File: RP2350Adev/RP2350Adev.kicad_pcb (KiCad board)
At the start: 2 copper layers, 32.6 x 53.6 mm, 44 parts, among them J1 USB4105-GF-A, J2 LEFT, J3 DEBUG, J4 RIGHT, U1 W25Q32JV, U2 RP2350A, U3 MCP1702T-3302E_CB, X1 IQXO-791

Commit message: Add files via upload
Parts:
- moved C10 0.30 mm to (156.9, 87.9)
- moved S2 0.29 mm to (148.4, 86.7)
- moved C17 0.18 mm to (155.3, 83.2)
- moved C11 0.15 mm to (156.9, 89.8)
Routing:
- net GND: track 88.4 -> 69.3 mm, vias 25 -> 22

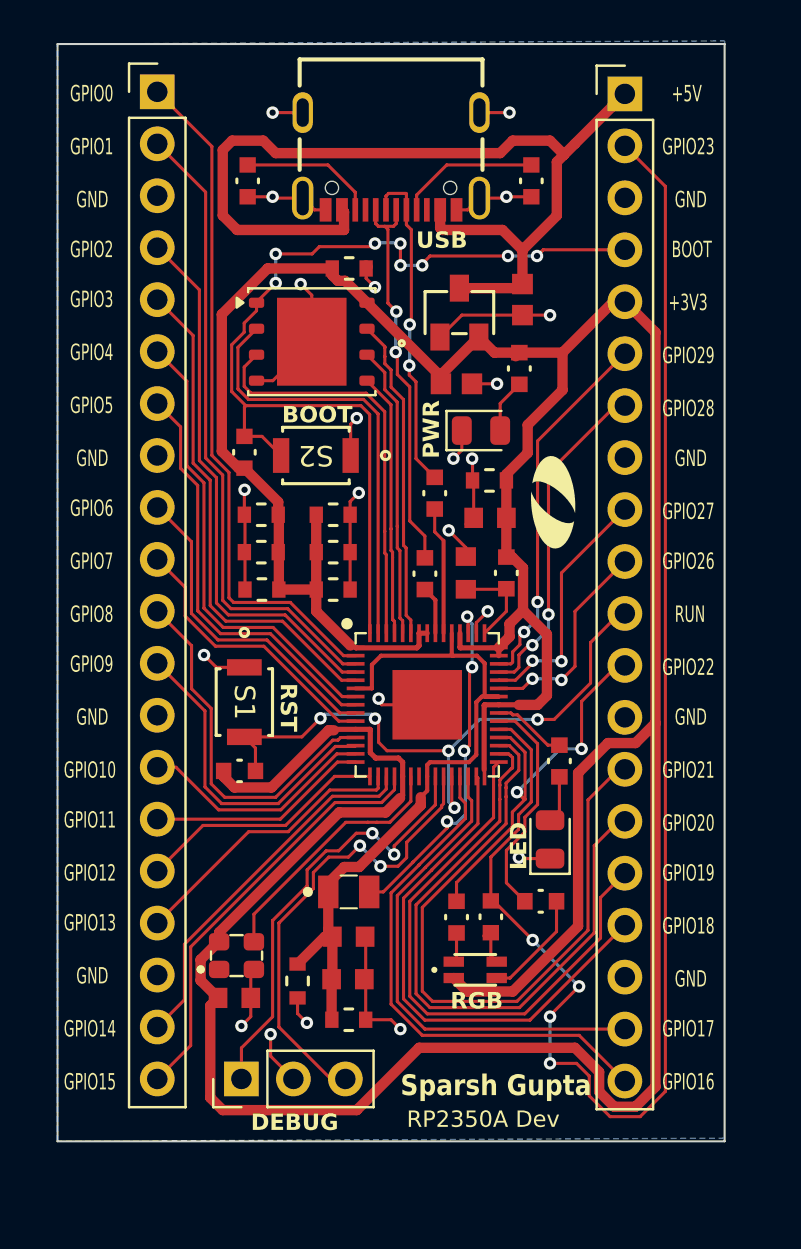
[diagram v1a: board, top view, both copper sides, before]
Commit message: update RP2350A board layout
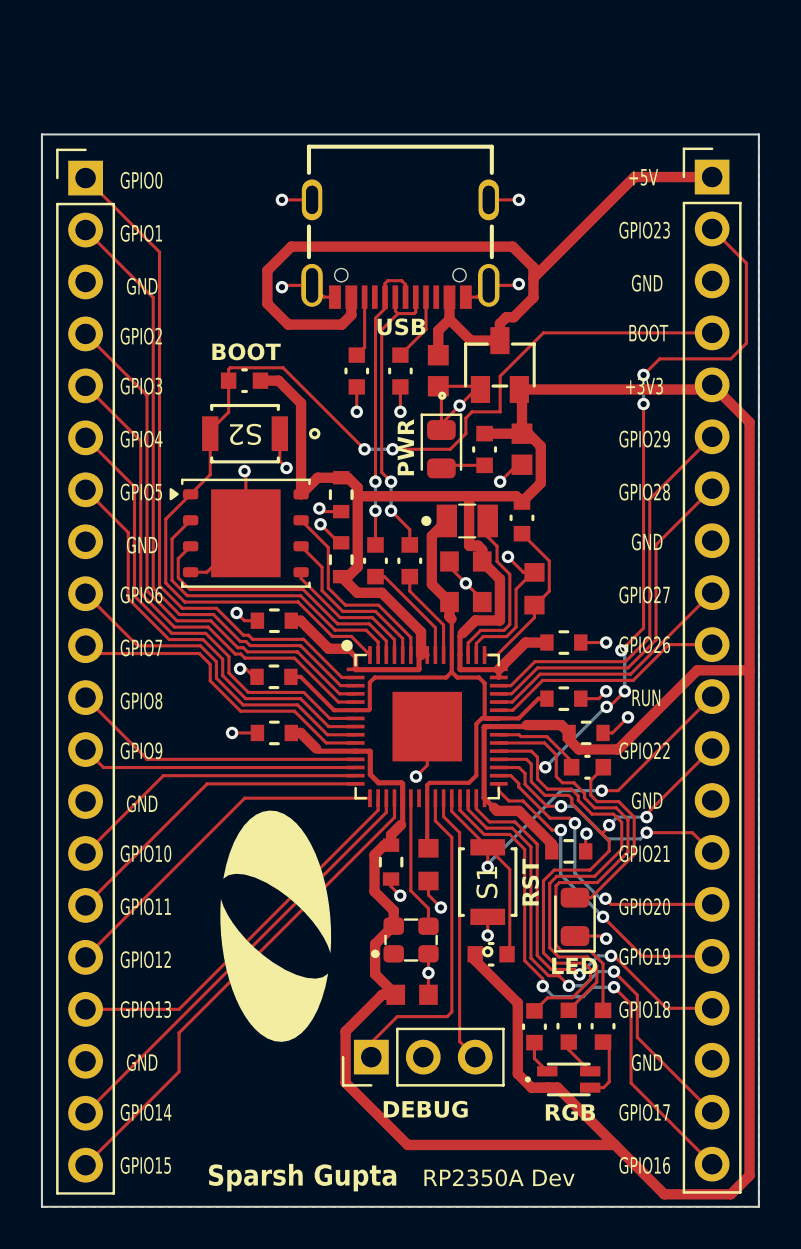
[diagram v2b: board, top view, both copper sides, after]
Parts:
- removed OlinLogoSm1: G***, Eclectronics:OlinLogoSm1
- added OlinLogoLg: G***, Eclectronics:OlinLogoLg, F.Cu at (146.5, 109.7)
- moved C7 22.3 mm to (160.8, 106.1), turned to 180 degrees
- moved L1 19.0 mm to (155.8, 89.9)
- moved C15 19.0 mm to (160.5, 98.6), turned to 180 degrees
- moved C8 18.2 mm to (161.6, 100.3), turned to 180 degrees
- moved C3 17.3 mm to (155.8, 93.9)
- moved C6 17.2 mm to (152.1, 106.6), turned to 90 degrees
- moved C13 17.2 mm to (146.4, 97.5), turned to 0 degrees
- moved R1 15.2 mm to (157.0, 111.1)
- moved C9 15.0 mm to (160.5, 95.9), turned to 180 degrees
- moved S1 14.8 mm to (156.8, 107.6), turned to 90 degrees
- moved R4 11.3 mm to (152.6, 82.6)
- moved C1 11.1 mm to (149.7, 88.6), turned to 90 degrees
- moved R3 10.7 mm to (150.4, 82.6)
- moved U1 9.90 mm to (145.0, 90.5)
- moved C5 9.29 mm to (146.4, 100.3), turned to 0 degrees
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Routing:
- net /GPIO21: track 33.2 -> 12.7 mm, vias 0 -> 2
- net /GPIO23: track 75.5 -> 56.0 mm, vias 4 -> 6
- net /GPIO20: track 31.0 -> 14.6 mm, vias 0 -> 2
- net /GPIO19: track 28.7 -> 15.4 mm, vias 0 -> 2
- net /GPIO24: track 11.1 -> 22.3 mm
- net GND: track 69.3 -> 59.0 mm, vias 22 -> 27
- net /SWDIO: track 23.0 -> 13.3 mm, vias 2 -> 0
- net +3V3: track 204.5 -> 195.1 mm
- net /GPIO22: track 20.0 -> 29.3 mm
- net Net-(U2-VREG_LX): track 17.5 -> 8.82 mm, vias 4 -> 0
- net Net-(D1-A): track 2.31 -> 9.97 mm
- net /RUN: track 32.0 -> 24.4 mm, vias 5 -> 2
- net Net-(U1-DO/IO1): track 21.4 -> 15.3 mm
- net Net-(U1-~{WP}/IO2): track 20.0 -> 13.9 mm
- net Net-(U1-DI/IO0): track 12.9 -> 6.86 mm
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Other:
- board size 32.6 x 53.6 mm -> 35.1 x 52.4 mm

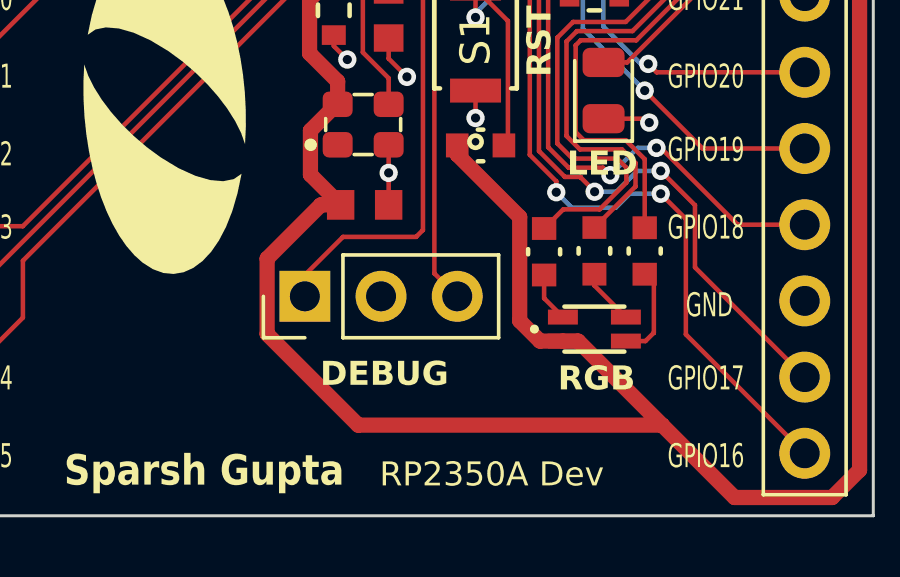
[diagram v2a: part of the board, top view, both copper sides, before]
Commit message: update RP2350A
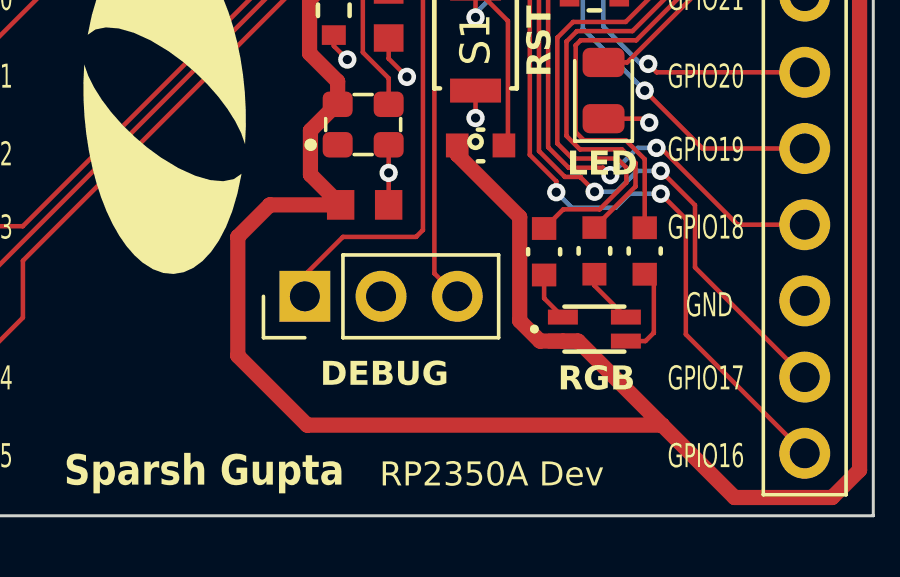
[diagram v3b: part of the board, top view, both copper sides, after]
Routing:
- net +3V3: track 195.1 -> 197.9 mm
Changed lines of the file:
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@@
-	)
-	(segment
-		(start 152.90835 120.42195)
-		(end 163.04205 120.42195)
-		(width 0.508)
-		(layer "F.Cu")
-		(net 1)
 	)
 	(segment
@@
 	)
 	(segment
+		(start 151.20675 120.42195)
+		(end 163.04205 120.42195)
+		(width 0.508)
+		(layer "F.Cu")
+		(net 1)
+	)
+	(segment
 		(start 158.653949 99.9692)
 		(end 158.728092 99.895057)
@@
 	)
 	(segment
+		(start 148.8948 118.11)
+		(end 151.20675 120.42195)
+		(width 0.508)
+		(layer "F.Cu")
+		(net 1)
+	)
+	(segment
 		(start 159.4134 86.2594)
 		(end 159.4134 88.0715)
@@
 	)
 	(segment
-		(start 149.8726 114.8714)
-		(end 149.8726 117.3862)
-		(width 0.508)
-		(layer "F.Cu")
-		(net 1)
-	)
-	(segment
 		(start 158.8028 85.6488)
 		(end 159.4134 86.2594)
@@
 	)
 	(segment
+		(start 152.3238 113.0808)
+		(end 149.9616 113.0808)
+		(width 0.508)
+		(layer "F.Cu")
+		(net 1)
+	)
+	(segment
 		(start 160.8028 100.610426)
 		(end 161.278974 101.0866)
@@
 	)
 	(segment
-		(start 152.3238 113.0808)
-		(end 151.6632 113.0808)
-		(width 0.508)
-		(layer "F.Cu")
-		(net 1)
-	)
-	(segment
 		(start 169.6212 85.09)
 		(end 167.7924 83.2612)
@@
 	)
 	(segment
+		(start 149.9616 113.0808)
+		(end 148.8948 114.1476)
+		(width 0.508)
+		(layer "F.Cu")
+		(net 1)
+	)
+	(segment
 		(start 155.9122 88.7086)
 		(end 158.2157 88.7086)
@@
 	)
 	(segment
-		(start 151.6632 113.0808)
-		(end 149.8726 114.8714)
-		(width 0.508)
-		(layer "F.Cu")
-		(net 1)
-	)
-	(segment
 		(start 145.710199 83.058)
 		(end 146.595998 83.058)
@@
 	)
 	(segment
-		(start 149.8726 117.3862)
-		(end 152.90835 120.42195)
-		(width 0.508)
-		(layer "F.Cu")
+		(start 148.8948 114.1476)
+		(end 148.8948 118.11)
+		(width 0.508)
+		(layer "F.Cu")
